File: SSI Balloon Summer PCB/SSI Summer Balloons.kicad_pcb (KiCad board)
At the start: 4 copper layers, 80 x 59 mm, 106 parts, among them J1 Battery connector, J2 Conn_01x02, J3 LoRa antenna, J4 APRS antenna, J5 Conn_01x05, J6 1040310811, J7 GPS antenna, J8 PT1000 Sensor, J9 Camera, Q2 DMG2305UX-7, SW2 SW_SPST, SW3 SW_SPST, U1 RFM95W-915S2, U10 MS5611-01BA03, U11 TPS63070RNMR, U12 TPS63070RNMR, U3 AP2112K-3.3TRG1, U4 ICM-42688-P, U5 DRA818V, U7 STM32F411CEUx, U8 MAX-M10S-00B, U9 MAX31865ATP_T, Y1 ABM8W-12.0000MHZ-8-K1Z-T3

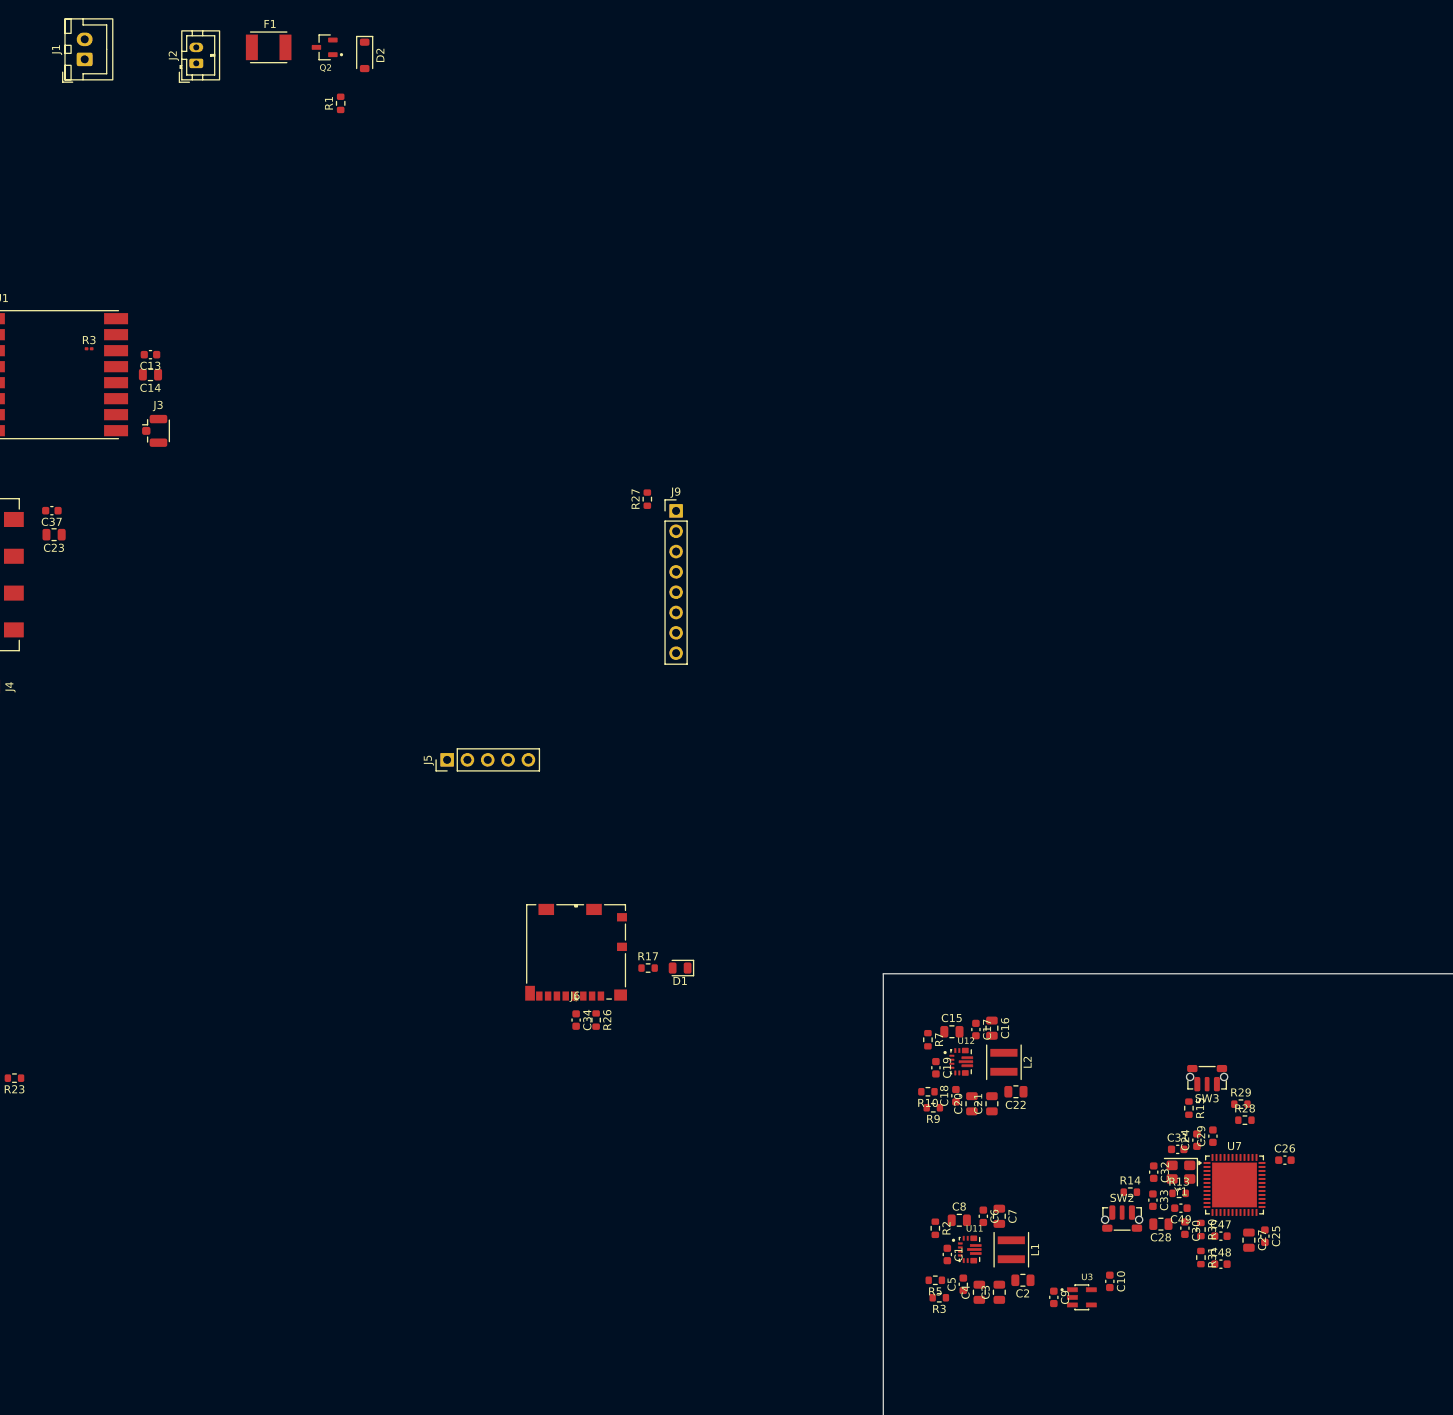
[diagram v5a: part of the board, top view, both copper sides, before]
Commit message: Routing for power sheet
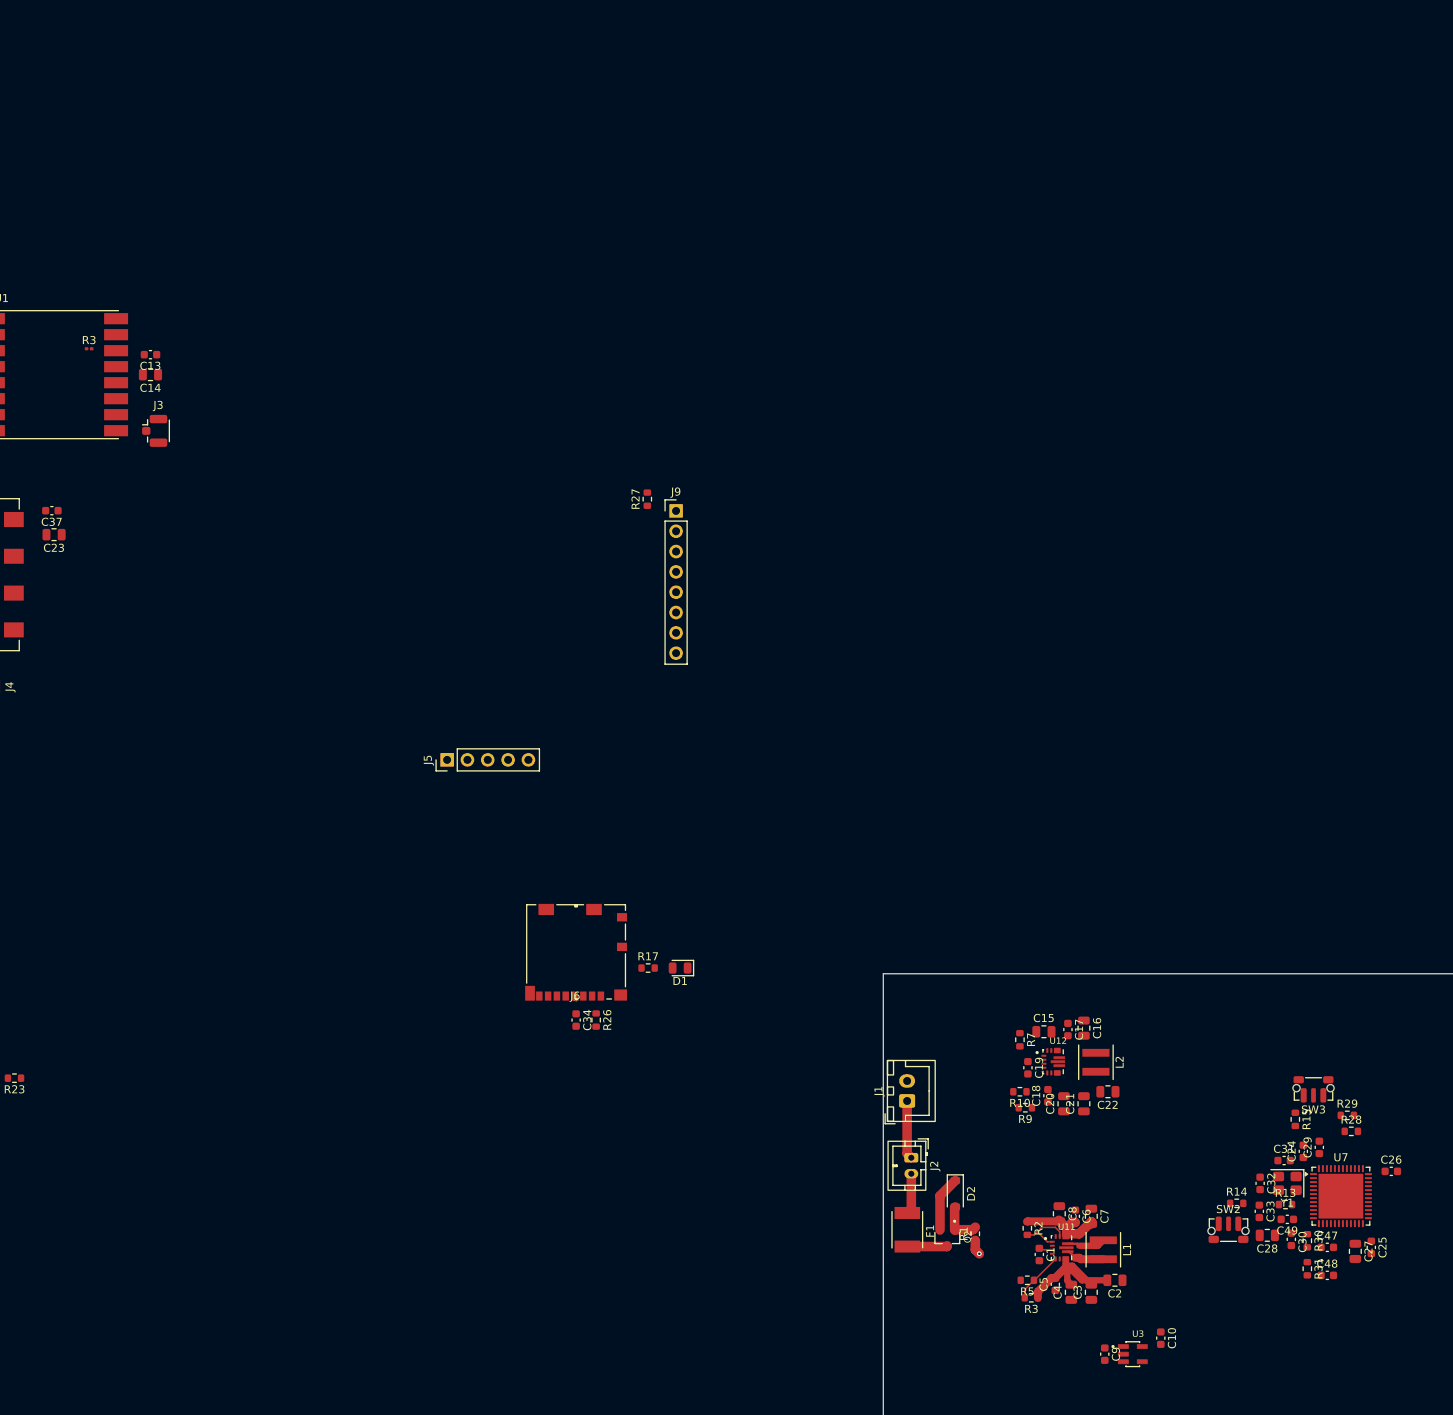
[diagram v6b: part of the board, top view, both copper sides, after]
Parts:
- moved F1 168.0 mm to (103.0, 110.5), turned to -90 degrees
- moved Q2 167.9 mm to (108.0, 111.5), turned to -90 degrees
- moved J1 165.9 mm to (103.0, 94.4)
- moved J2 163.4 mm to (103.5, 101.5), turned to -90 degrees
- moved R1 162.0 mm to (111.5, 111.0)
- moved D2 160.3 mm to (109.0, 106.0)
- moved C24 13.4 mm to (152.5, 100.7)
- moved C25 13.4 mm to (161.0, 112.7)
- moved C26 13.4 mm to (163.5, 103.2)
- moved C27 13.4 mm to (159.0, 113.2)
- moved C28 13.4 mm to (148.0, 111.2)
- moved C29 13.4 mm to (154.5, 100.2)
- moved C30 13.4 mm to (151.0, 111.7)
- moved C33 13.4 mm to (147.0, 108.2)
- moved C47 13.4 mm to (155.5, 112.7)
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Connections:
- F1 pad 1: Net-(SW1-A) -> Net-(J2-Pin_2)
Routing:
- net +5V: track 0.00 -> 18.8 mm
- net VBAT_PROT: track 0.00 -> 18.4 mm
- net Net-(U11-EN): track 0.00 -> 7.66 mm
- net VBAT: track 0.00 -> 7.32 mm
- net Net-(U11-FB): track 0.00 -> 6.49 mm
- net Net-(D2-A): track 0.00 -> 5.60 mm
- net Net-(J2-Pin_2): track 0.00 -> 5.11 mm
- net Net-(F1-Pad2): track 0.00 -> 5.02 mm
- net Net-(U11-L2): track 0.00 -> 4.84 mm
- net Net-(U11-L1): track 0.00 -> 4.84 mm
- net GND: track 0.00 -> 1.88 mm, vias 0 -> 1
- net Net-(U11-VAUX): track 0.00 -> 1.70 mm

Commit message: Routed 4v1 and 3v3 rail
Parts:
- moved C9 1.93 mm to (127.8, 128.0), turned to 90 degrees
- moved C15 1.19 mm to (121.0, 85.0), turned to -90 degrees
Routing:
- net +4V1: track 0.00 -> 21.1 mm
- net +5V: track 18.8 -> 30.3 mm
- net VBAT_PROT: track 18.4 -> 28.6 mm
- net Net-(U12-EN): track 0.00 -> 8.28 mm
- net Net-(U12-FB): track 0.00 -> 5.98 mm
- net Net-(U12-L2): track 0.00 -> 4.21 mm
- net Net-(U12-L1): track 0.00 -> 4.15 mm
- net +3V3: track 0.00 -> 2.43 mm
- net Net-(U12-VAUX): track 0.00 -> 2.11 mm

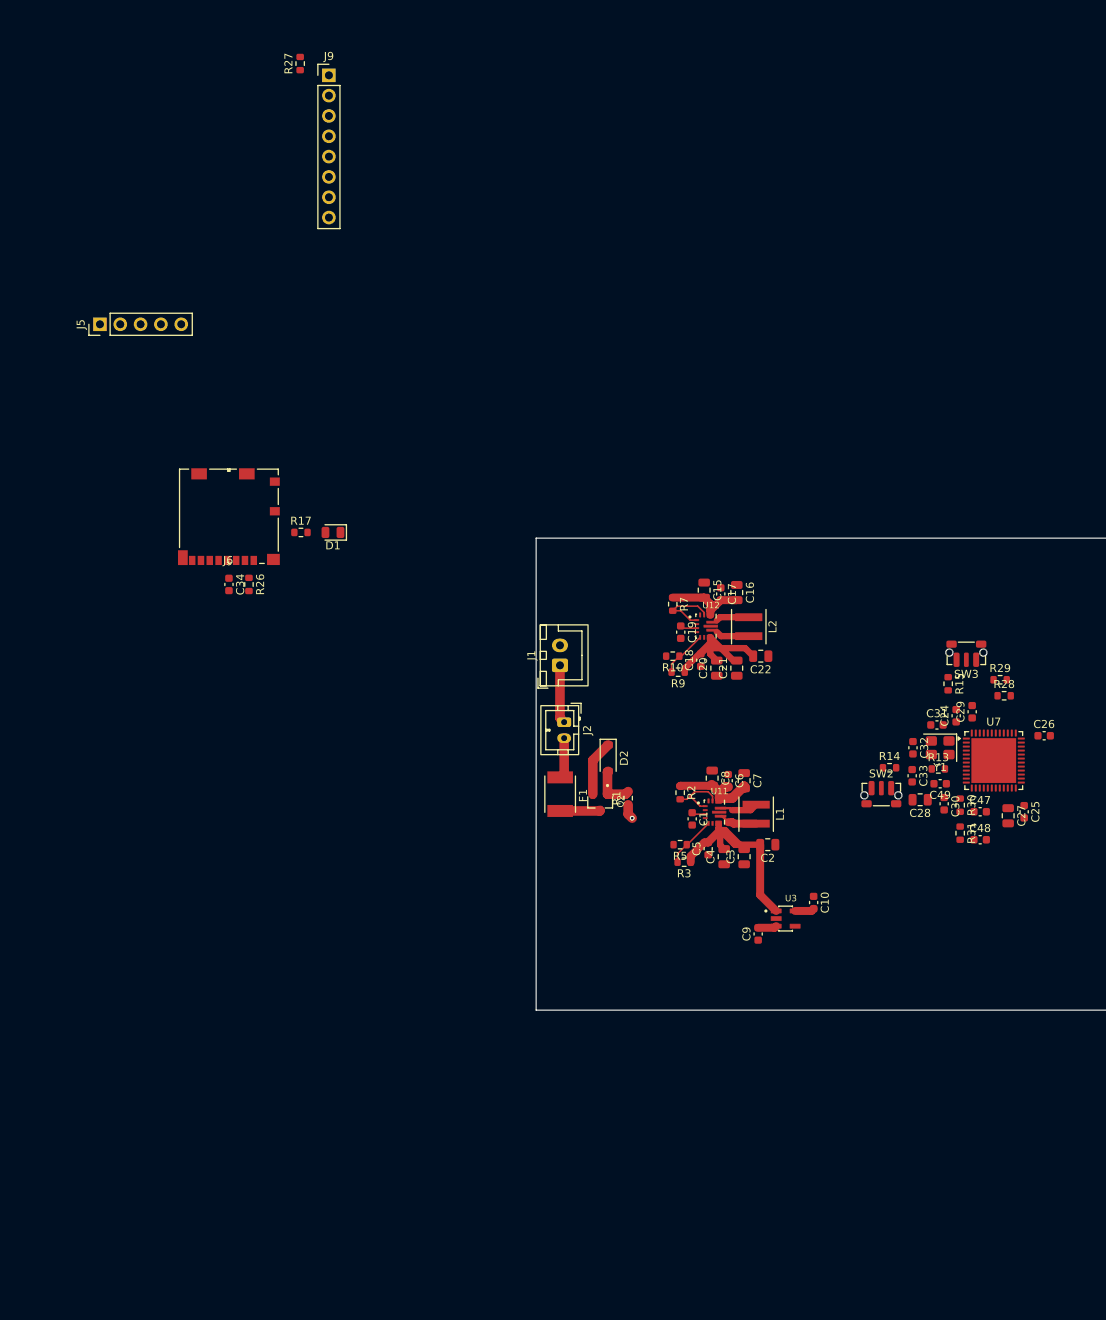
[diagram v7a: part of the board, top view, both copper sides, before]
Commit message: Halfway done connecting MCU traces
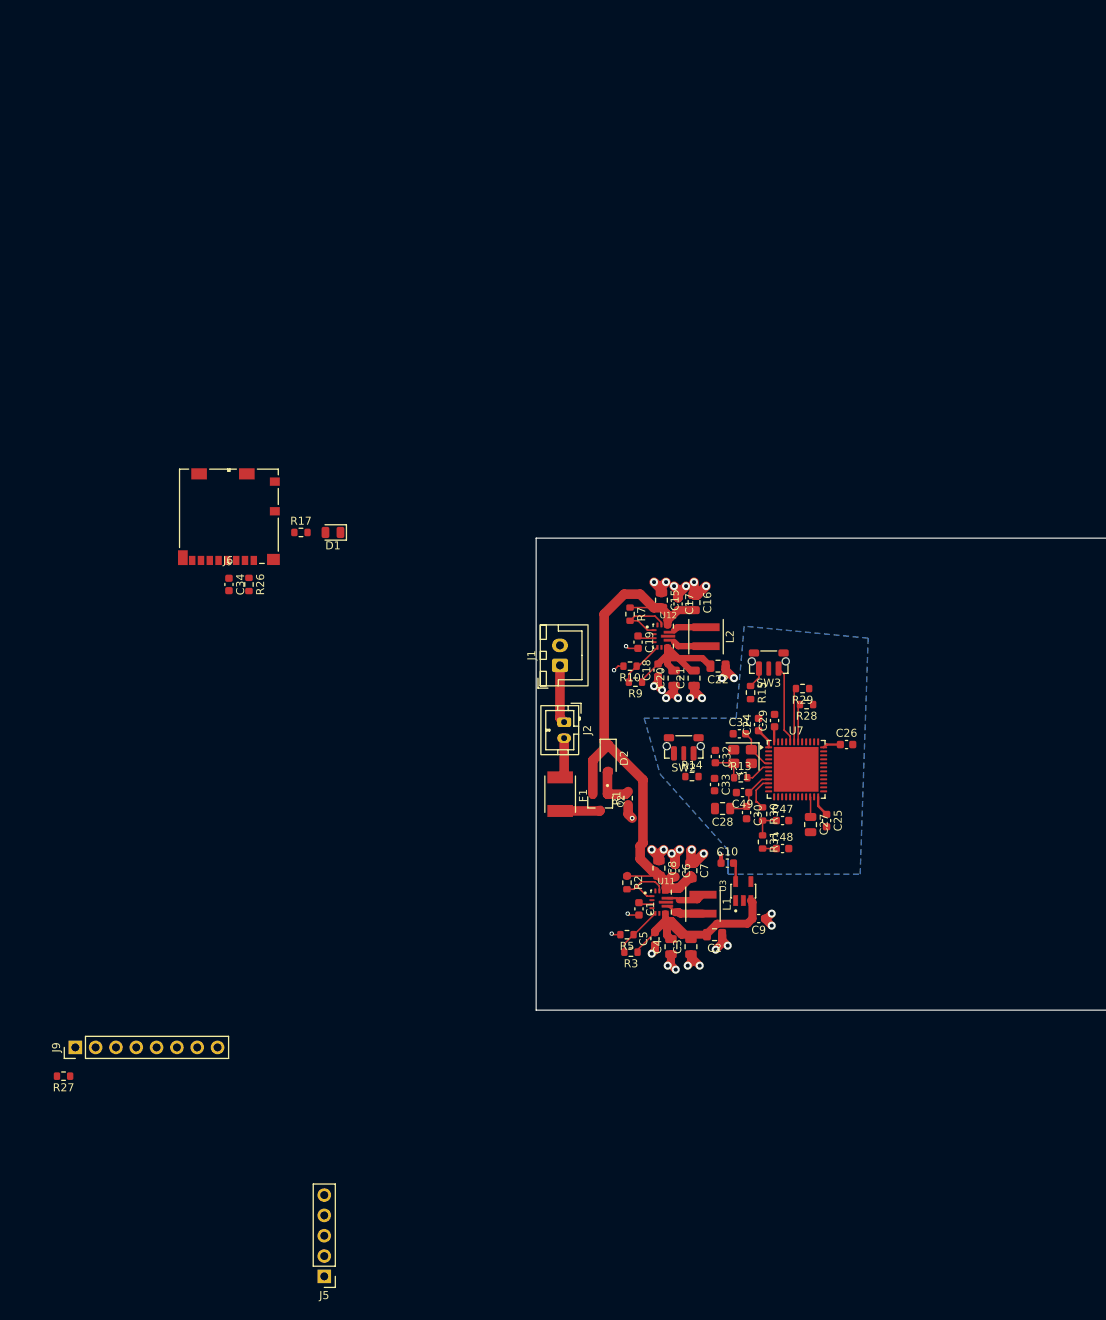
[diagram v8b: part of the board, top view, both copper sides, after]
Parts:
- moved R27 130.0 mm to (40.9, 145.8), turned to 180 degrees
- moved J9 125.6 mm to (42.4, 142.2), turned to 90 degrees
- moved J5 122.3 mm to (73.5, 170.8), turned to 180 degrees
- moved SW2 25.5 mm to (118.5, 104.5), turned to 180 degrees
- moved R14 24.7 mm to (119.5, 108.3)
- moved SW3 24.7 mm to (129.1, 93.9)
- moved C24 24.7 mm to (127.8, 101.8)
- moved C28 24.7 mm to (123.3, 112.3)
- moved C30 24.7 mm to (126.3, 112.8)
- moved C33 24.7 mm to (122.3, 109.3)
- moved C49 24.7 mm to (125.8, 110.3)
- moved R13 24.7 mm to (125.6, 108.5)
- moved R15 24.7 mm to (126.8, 97.8)
- moved Y1 24.7 mm to (125.8, 105.8)
- moved C25 24.7 mm to (136.3, 113.8)
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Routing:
- net GND: track 1.88 -> 58.8 mm, vias 1 -> 35
- net VBAT_PROT: track 28.6 -> 73.5 mm
- net +3V3: track 2.43 -> 19.0 mm
- net /MCU (STM)/BOOT0: track 0.00 -> 12.4 mm
- net /MCU (STM)/SDA: track 0.00 -> 6.76 mm
- net /MCU (STM)/OSC_IN: track 0.00 -> 5.17 mm
- net /MCU (STM)/SCL: track 0.00 -> 4.76 mm
- net Net-(U7-PA0): track 0.00 -> 4.48 mm
- net Net-(C32-Pad2): track 0.00 -> 4.15 mm
- net Net-(C47-Pad1): track 0.00 -> 3.58 mm
- net /MCU (STM)/OSC_OUT: track 0.00 -> 3.20 mm
- net Net-(U7-VCAP1): track 0.00 -> 2.53 mm
- net +5V: track 30.3 -> 27.8 mm
- net +4V1: track 21.1 -> 19.2 mm
- net /MCU (STM)/APRS_AUDIO: track 0.00 -> 1.72 mm
- added copper zone on B.Cu, net +3V3
